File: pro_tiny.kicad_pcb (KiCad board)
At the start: 2 copper layers, 12.5 x 24.1 mm, 24 parts, among them J1 Conn_01x12, J2 Conn_01x12, J3 Conn_01x04, J4 USB_C_Receptacle_USB2.0, U1 ATmega32U4-M, Y1 16mhz

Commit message: board updates and readme
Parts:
- moved FB1 0.15 mm to (97.2, 46.0)
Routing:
- net VBUS: track 7.96 -> 12.8 mm, vias 2 -> 3
- net Net-(J4-PadA7): track 0.90 -> 3.52 mm
- net D+: track 6.94 -> 9.18 mm
- net RST: track 0.00 -> 1.81 mm
- net Net-(C6-Pad2): track 0.00 -> 1.68 mm
- net Net-(C5-Pad2): track 0.00 -> 1.40 mm
- net +5V: track 14.2 -> 15.6 mm
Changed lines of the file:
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@@
     (fp_line (start 3.5 -3.5) (end 3.5 3.5) (layer "F.Fab") (width 0.1))
     (fp_line (start -2.5 -3.5) (end 3.5 -3.5) (layer "F.Fab") (width 0.1))
-    (pad "" smd roundrect (at 1.95 1.95 270) (size 1.05 1.05) (layers "F.Paste") (roundrect_rratio 0.238095))
-    (pad "" smd roundrect (at -1.95 0.65 270) (size 1.05 1.05) (layers "F.Paste") (roundrect_rratio 0.238095))
-    (pad "" smd roundrect (at -0.65 0.65 270) (size 1.05 1.05) (layers "F.Paste") (roundrect_rratio 0.238095))
-    (pad "" smd roundrect (at -0.65 -1.95 270) (size 1.05 1.05) (layers "F.Paste") (roundrect_rratio 0.238095))
-    (pad "" smd roundrect (at 0.65 1.95 270) (size 1.05 1.05) (layers "F.Paste") (roundrect_rratio 0.238095))
-    (pad "" smd roundrect (at -1.95 1.95 270) (size 1.05 1.05) (layers "F.Paste") (roundrect_rratio 0.238095))
-    (pad "" smd roundrect (at -1.95 -1.95 270) (size 1.05 1.05) (layers "F.Paste") (roundrect_rratio 0.238095))
-    (pad "" smd roundrect (at 1.95 -0.65 270) (size 1.05 1.05) (layers "F.Paste") (roundrect_rratio 0.238095))
-    (pad "" smd roundrect (at -0.65 -0.65 270) (size 1.05 1.05) (layers "F.Paste") (roundrect_rratio 0.238095))
-    (pad "" smd roundrect (at 1.95 -1.95 270) (size 1.05 1.05) (layers "F.Paste") (roundrect_rratio 0.238095))
-    (pad "" smd roundrect (at 1.95 0.65 270) (size 1.05 1.05) (layers "F.Paste") (roundrect_rratio 0.238095))
-    (pad "" smd roundrect (at 0.65 0.65 270) (size 1.05 1.05) (layers "F.Paste") (roundrect_rratio 0.238095))
-    (pad "" smd roundrect (at 0.65 -0.65 270) (size 1.05 1.05) (layers "F.Paste") (roundrect_rratio 0.238095))
-    (pad "" smd roundrect (at 0.65 -1.95 270) (size 1.05 1.05) (layers "F.Paste") (roundrect_rratio 0.238095))
-    (pad "" smd roundrect (at -1.95 -0.65 270) (size 1.05 1.05) (layers "F.Paste") (roundrect_rratio 0.238095))
-    (pad "" smd roundrect (at -0.65 1.95 270) (size 1.05 1.05) (layers "F.Paste") (roundrect_rratio 0.238095))
     (pad "1" smd roundrect (at -3.3375 -2.5 270) (size 1.075 0.25) (layers "F.Cu" "F.Paste" "F.Mask") (roundrect_rratio 0.25)
       (net 24 "D7") (pinfunction "PE6") (pintype "bidirectional"))
@@
     (pad "44" smd roundrect (at -2.5 -3.3375 270) (size 0.25 1.075) (layers "F.Cu" "F.Paste" "F.Mask") (roundrect_rratio 0.25)
       (net 3 "Net-(C2-Pad2)") (pinfunction "AVCC") (pintype "passive"))
-    (pad "45" smd rect (at 0 0 270) (size 5.2 5.2) (layers "F.Cu" "F.Mask")
-      (net 2 "GND") (pinfunction "GND") (pintype "passive"))
     (model "${KICAD6_3DMODEL_DIR}/Package_DFN_QFN.3dshapes/QFN-44-1EP_7x7mm_P0.5mm_EP5.2x5.2mm.wrl"
       (offset (xyz 0 0 0))
@@
   )
   (footprint "Resistor_SMD:R_0402_1005Metric" (layer "F.Cu")
-    (at 97.25 45.85 180)
+    (at 97.25 46 180)
     (descr "Resistor SMD 0402 (1005 Metric), square (rectangular) end terminal, IPC_7351 nominal, (Body size source: IPC-SM-782 page 72, https://www.pcb-3d.com/wordpress/wp-content/uploads/ipc-sm-782a_amendment_1_and_2.pdf), generated with kicad-footprint-generator")
     (tags "resistor")
@@
   (segment (start 102.04 44.95) (end 102.5 44.49) (width 0.127) (layer "F.Cu") (net 1))
   (segment (start 102.4 43.4) (end 102.4 42.705) (width 0.127) (layer "F.Cu") (net 1))
+  (via (at 97.6 42.75) (size 0.5) (drill 0.3) (layers "F.Cu" "B.Cu") (net 1))
   (via (at 99.5 47.25) (size 0.5) (drill 0.3) (layers "F.Cu" "B.Cu") (net 1))
   (via (at 102.06 45.9) (size 0.5) (drill 0.3) (layers "F.Cu" "B.Cu") (net 1))
+  (segment (start 98.40691 43.35) (end 97.6 43.35) (width 0.127) (layer "B.Cu") (net 1))
   (segment (start 102.06 45.9) (end 101.71 46.25) (width 0.127) (layer "B.Cu") (net 1))
   (segment (start 101.71 46.25) (end 99.75 46.25) (width 0.127) (layer "B.Cu") (net 1))
+  (segment (start 98.7635 43.70659) (end 98.40691 43.35) (width 0.127) (layer "B.Cu") (net 1))
+  (segment (start 97.6 43.35) (end 97.6 42.75) (width 0.127) (layer "B.Cu") (net 1))
+  (segment (start 98.7635 45.2635) (end 98.7635 43.70659) (width 0.127) (layer "B.Cu") (net 1))
   (segment (start 99.75 46.25) (end 99.5 46.5) (width 0.127) (layer "B.Cu") (net 1))
   (segment (start 99.5 46.5) (end 99.5 47.25) (width 0.127) (layer "B.Cu") (net 1))
-  (segment (start 101.7635 46.4635) (end 102 46.4635) (width 0.127) (layer "F.Cu") (net 4))
+  (segment (start 99.75 46.25) (end 98.7635 45.2635) (width 0.127) (layer "B.Cu") (net 1))
+  (segment (start 102 46.4635) (end 101.7635 46.4635) (width 0.127) (layer "F.Cu") (net 4))
+  (segment (start 98.1175 46.4325) (end 98.004 46.546) (width 0.127) (layer "F.Cu") (net 4))
   (segment (start 103.95 46.4) (end 103.95 45.93) (width 0.127) (layer "F.Cu") (net 4))
-  (segment (start 101.6705 46.3705) (end 101.7635 46.4635) (width 0.127) (layer "F.Cu") (net 4))
   (segment (start 102 48.2125) (end 102 46.45) (width 0.127) (layer "F.Cu") (net 4))
+  (segment (start 98.004 46.546) (end 97.286 46.546) (width 0.127) (layer "F.Cu") (net 4))
   (segment (start 105.6865 45.6635) (end 105.42 45.93) (width 0.127) (layer "F.Cu") (net 4))
+  (segment (start 97.286 46.546) (end 96.74 46) (width 0.127) (layer "F.Cu") (net 4))
+  (segment (start 101.7325 46.4325) (end 98.1175 46.4325) (width 0.127) (layer "F.Cu") (net 4))
   (segment (start 105.6865 45.5365) (end 105.6865 45.6635) (width 0.127) (layer "F.Cu") (net 4))
   (segment (start 103.95 44.13) (end 104.28 44.13) (width 0.127) (layer "F.Cu") (net 4))
   (segment (start 102 46.45) (end 103.9 46.45) (width 0.127) (layer "F.Cu") (net 4))
-  (segment (start 96.74 46.24) (end 96.8705 46.3705) (width 0.127) (layer "F.Cu") (net 4))
   (segment (start 103.9 46.45) (end 103.95 46.4) (width 0.127) (layer "F.Cu") (net 4))
   (segment (start 105.42 45.93) (end 103.95 45.93) (width 0.127) (layer "F.Cu") (net 4))
-  (segment (start 96.8705 46.3705) (end 101.6705 46.3705) (width 0.127) (layer "F.Cu") (net 4))
+  (segment (start 97.8 58.64) (end 96.3225 58.64) (width 0.127) (layer "F.Cu") (net 4))
+  (segment (start 96.3225 58.64) (end 96.25 58.7125) (width 0.127) (layer "F.Cu") (net 4))
   (segment (start 104.28 44.13) (end 105.6865 45.5365) (width 0.127) (layer "F.Cu") (net 4))
-  (segment (start 96.74 45.85) (end 96.74 46.24) (width 0.127) (layer "F.Cu") (net 4))
+  (segment (start 101.7635 46.4635) (end 101.7325 46.4325) (width 0.127) (layer "F.Cu") (net 4))
+  (segment (start 100.95 56.95) (end 102.07 56.95) (width 0.127) (layer "F.Cu") (net 5))
+  (segment (start 102.07 56.95) (end 102.27 56.75) (width 0.127) (layer "F.Cu") (net 5))
+  (segment (start 98.32 58.05) (end 98 57.73) (width 0.127) (layer "F.Cu") (net 6))
+  (segment (start 99.55 58.05) (end 98.32 58.05) (width 0.127) (layer "F.Cu") (net 6))
+  (segment (start 97.1725 60.2875) (end 97.8 59.66) (width 0.127) (layer "F.Cu") (net 9))
+  (segment (start 96.25 60.2875) (end 97.1725 60.2875) (width 0.127) (layer "F.Cu") (net 9))
   (segment (start 105.45 51.05) (end 105.5 51) (width 0.127) (layer "F.Cu") (net 12))
   (segment (start 103.3375 51.05) (end 105.45 51.05) (width 0.127) (layer "F.Cu") (net 12))
@@
   (segment (start 98.2 44) (end 97.25 44.95) (width 0.127) (layer "B.Cu") (net 16))
   (segment (start 99.85 44.89) (end 100.75 44.89) (width 0.127) (layer "F.Cu") (net 17))
-  (segment (start 96.734173 46.6245) (end 96.2795 46.169827) (width 0.127) (layer "F.Cu") (net 22))
+  (segment (start 100.75 44.89) (end 101.2705 44.3695) (width 0.127) (layer "F.Cu") (net 17))
+  (segment (start 100.750447 43.143899) (end 100.750447 42.705) (width 0.127) (layer "F.Cu") (net 17))
+  (segment (start 101.2705 44.3695) (end 101.2705 43.663952) (width 0.127) (layer "F.Cu") (net 17))
+  (segment (start 101.2705 43.663952) (end 100.750447 43.143899) (width 0.127) (layer "F.Cu") (net 17))
+  (segment (start 97.529673 45.45) (end 98.2 45.45) (width 0.127) (layer "F.Cu") (net 22))
+  (segment (start 99.15309 46.8) (end 96.65 46.8) (width 0.127) (layer "F.Cu") (net 22))
+  (segment (start 96.65 46.8) (end 96.25 46.4) (width 0.127) (layer "F.Cu") (net 22))
+  (segment (start 97.01659 45.5135) (end 97.466173 45.5135) (width 0.127) (layer "F.Cu") (net 22))
   (segment (start 101 48.2125) (end 101 47.817204) (width 0.127) (layer "F.Cu") (net 22))
-  (segment (start 101 47.817204) (end 99.807296 46.6245) (width 0.127) (layer "F.Cu") (net 22))
-  (segment (start 96.25 45.55) (end 96.1 45.4) (width 0.127) (layer "F.Cu") (net 22))
-  (segment (start 99.807296 46.6245) (end 99.2 46.6245) (width 0.127) (layer "F.Cu") (net 22))
-  (segment (start 96.1 45.4) (end 95.8 45.4) (width 0.127) (layer "F.Cu") (net 22))
-  (segment (start 96.25 46.140327) (end 96.25 45.55) (width 0.127) (layer "F.Cu") (net 22))
-  (segment (start 96.2795 46.169827) (end 96.25 46.140327) (width 0.127) (layer "F.Cu") (net 22))
-  (segment (start 99.2 46.6245) (end 96.734173 46.6245) (width 0.127) (layer "F.Cu") (net 22))
+  (segment (start 96.3105 45.4895) (end 96.99259 45.4895) (width 0.127) (layer "F.Cu") (net 22))
+  (segment (start 98.2 45.45) (end 98.2 44.96) (width 0.127) (layer "F.Cu") (net 22))
+  (segment (start 96.25 46.4) (end 96.25 45.55) (width 0.127) (layer "F.Cu") (net 22))
+  (segment (start 99.869296 46.6865) (end 99.26659 46.6865) (width 0.127) (layer "F.Cu") (net 22))
+  (segment (start 99.26659 46.6865) (end 99.15309 46.8) (width 0.127) (layer "F.Cu") (net 22))
+  (segment (start 101 47.817204) (end 99.869296 46.6865) (width 0.127) (layer "F.Cu") (net 22))
+  (segment (start 96.99259 45.4895) (end 97.01659 45.5135) (width 0.127) (layer "F.Cu") (net 22))
+  (segment (start 97.466173 45.5135) (end 97.529673 45.45) (width 0.127) (layer "F.Cu") (net 22))
+  (segment (start 96.25 45.55) (end 96.3105 45.4895) (width 0.127) (layer "F.Cu") (net 22))
   (segment (start 105.5 53.05) (end 105.5 53.75) (width 0.127) (layer "F.Cu") (net 40))
   (segment (start 106.1865 54.4365) (end 106.1865 54.49) (width 0.127) (layer "F.Cu") (net 40))

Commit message: bit of everything
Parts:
- moved C2 11.6 mm to (104.6, 49.3)
- moved C8 10.3 mm to (95.5, 46.9)
- moved D1 8.27 mm to (100.0, 52.1)
- moved R6 8.27 mm to (101.6, 51.8)
- moved C6 0.25 mm to (97.8, 57.0)
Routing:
- net RST: track 1.81 -> 12.2 mm, vias 0 -> 1
- net Net-(C7-Pad1): track 0.00 -> 10.1 mm, vias 0 -> 2
- net Net-(C2-Pad2): track 0.00 -> 9.55 mm, vias 0 -> 2
- net Net-(C8-Pad2): track 0.00 -> 7.25 mm, vias 0 -> 2
- net D-: track 0.00 -> 3.30 mm, vias 0 -> 2
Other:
- board size 12.5 x 24.1 mm -> 13.8 x 24.1 mm

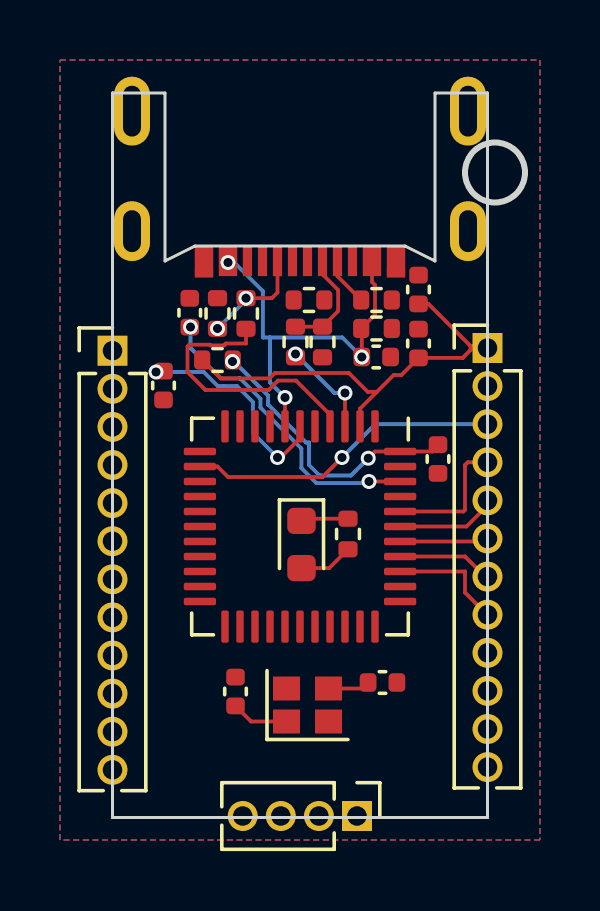
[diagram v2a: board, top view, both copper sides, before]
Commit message: finished routing main pins
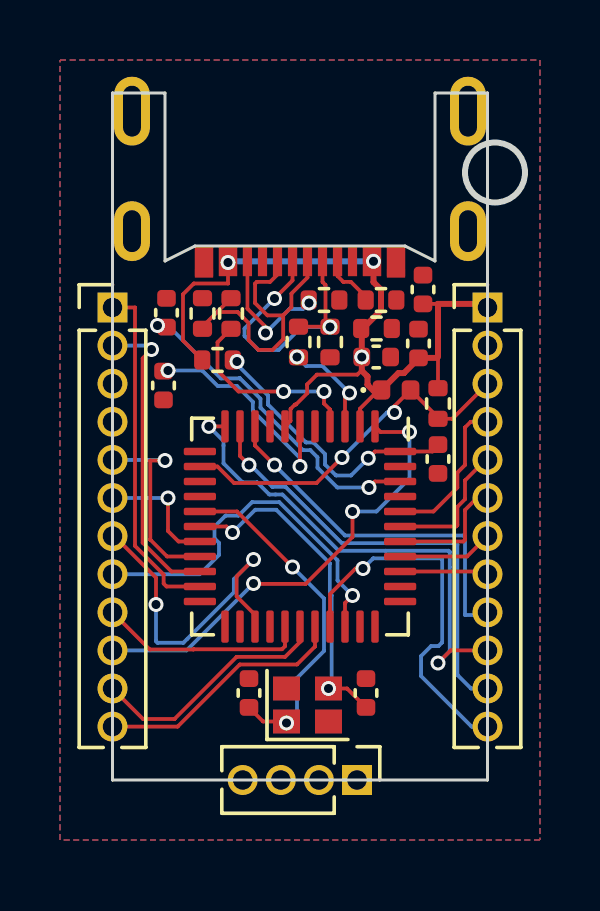
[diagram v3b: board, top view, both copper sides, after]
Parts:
- D1: footprint Diode_SMD:D_0603_1608Metric -> Diode_SMD:D_0402_1005Metric
- moved D1 6.04 mm to (103.2, 47.0), turned to 0 degrees
- moved R6 5.28 mm to (104.6, 47.5)
- moved J1 1.44 mm to (93.8, 44.2)
- moved J2 1.35 mm to (106.2, 44.2)
- moved J3 1.20 mm to (101.9, 60.0)
- moved C7 0.78 mm to (95.5, 44.4)
- moved C5 0.65 mm to (102.2, 57.1), turned to -90 degrees
- moved R1 0.50 mm to (97.7, 44.5)
- moved R4 0.50 mm to (100.8, 44.0)
- moved RV2 0.50 mm to (96.8, 44.5)
- moved C6 0.45 mm to (98.3, 57.1)
- moved RV1 0.25 mm to (101.0, 45.4)
- moved R5 0.15 mm to (102.7, 44.0)
- moved C3 0.15 mm to (104.1, 43.6)
- moved R2 0.10 mm to (100.0, 45.4)
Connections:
- C3 pad 2: +5V -> VBUS
- C4 pad 1: +5V -> VBUS
- D1 pad 1: +5V -> VBUS
- FB1 pad 2: +5V -> VBUS
- J2 pad 1: +5V -> VBUS
- R6 pad 1: +5V -> VBUS
- U1 pad 14: +5V -> VBUS
- U1 pad 2: +5V -> VBUS
- U1 pad 34: +5V -> VBUS
- Y1 pad 3: GND -> (no net)
- Y1 pad 4: GND -> (no net)
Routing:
- net D14/MISO: track 0.00 -> 16.5 mm, vias 0 -> 2
- net +5V: track 16.0 -> 0.00 mm
- net D7: track 0.00 -> 15.5 mm, vias 0 -> 3
- net D16/MOSI: track 0.00 -> 14.9 mm, vias 0 -> 1
- net VBUS: track 13.3 -> 27.3 mm
- net IO10: track 0.00 -> 12.6 mm, vias 0 -> 1
- net D5: track 0.00 -> 12.5 mm, vias 0 -> 1
- net D15/SCK: track 0.00 -> 12.3 mm, vias 0 -> 1
- net D1/TX: track 0.00 -> 11.5 mm
- net D4: track 0.00 -> 11.5 mm, vias 0 -> 2
- net D0/RX: track 0.00 -> 10.2 mm, vias 0 -> 1
- net Net-(C5-Pad2): track 1.40 -> 11.2 mm, vias 0 -> 2
- net Net-(C6-Pad2): track 1.92 -> 11.5 mm, vias 0 -> 2
- net IO9: track 0.00 -> 8.45 mm
- net IO8: track 0.00 -> 8.22 mm
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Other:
- board size 13.8 x 24.1 mm -> 13.8 x 22.9 mm

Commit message: finished routing and more
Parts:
- moved C5 3.90 mm to (98.3, 57.1), turned to 90 degrees
- moved C6 3.90 mm to (102.2, 57.1)
- moved J3 0.60 mm to (101.9, 59.4)
- moved C8 0.53 mm to (95.8, 46.5)
- moved C7 0.25 mm to (95.8, 44.4)
- moved Y1 0.20 mm to (100.2, 57.3)
- moved C2 0.11 mm to (104.7, 49.4)
- moved R1 0.08 mm to (97.8, 44.5)
- moved RV2 0.08 mm to (96.8, 44.5)
- moved R6 0.07 mm to (104.7, 47.5)
- moved C4 0.07 mm to (104.0, 45.5)
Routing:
- net A5: track 0.00 -> 18.8 mm, vias 0 -> 2
- net IO11: track 0.00 -> 15.6 mm, vias 0 -> 1
- net IO12: track 0.00 -> 9.73 mm, vias 0 -> 1
- net IO13: track 0.00 -> 6.33 mm
- net GND: track 0.06 -> 4.55 mm, vias 0 -> 13
- net Net-(C6-Pad2): track 11.5 -> 15.6 mm
- net D4: track 11.5 -> 7.97 mm
- net D14/MISO: track 16.5 -> 14.2 mm
- net IO10: track 12.6 -> 10.3 mm
- net IO9: track 8.45 -> 10.6 mm
- net D7: track 15.5 -> 17.6 mm
- net D5: track 12.5 -> 11.1 mm
- net D16/MOSI: track 14.9 -> 13.6 mm
- net D15/SCK: track 12.3 -> 11.4 mm
- net IO8: track 8.22 -> 9.08 mm
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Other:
- board size 13.8 x 22.9 mm -> 12.5 x 23.1 mm
